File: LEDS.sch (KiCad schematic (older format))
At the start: 8 parts

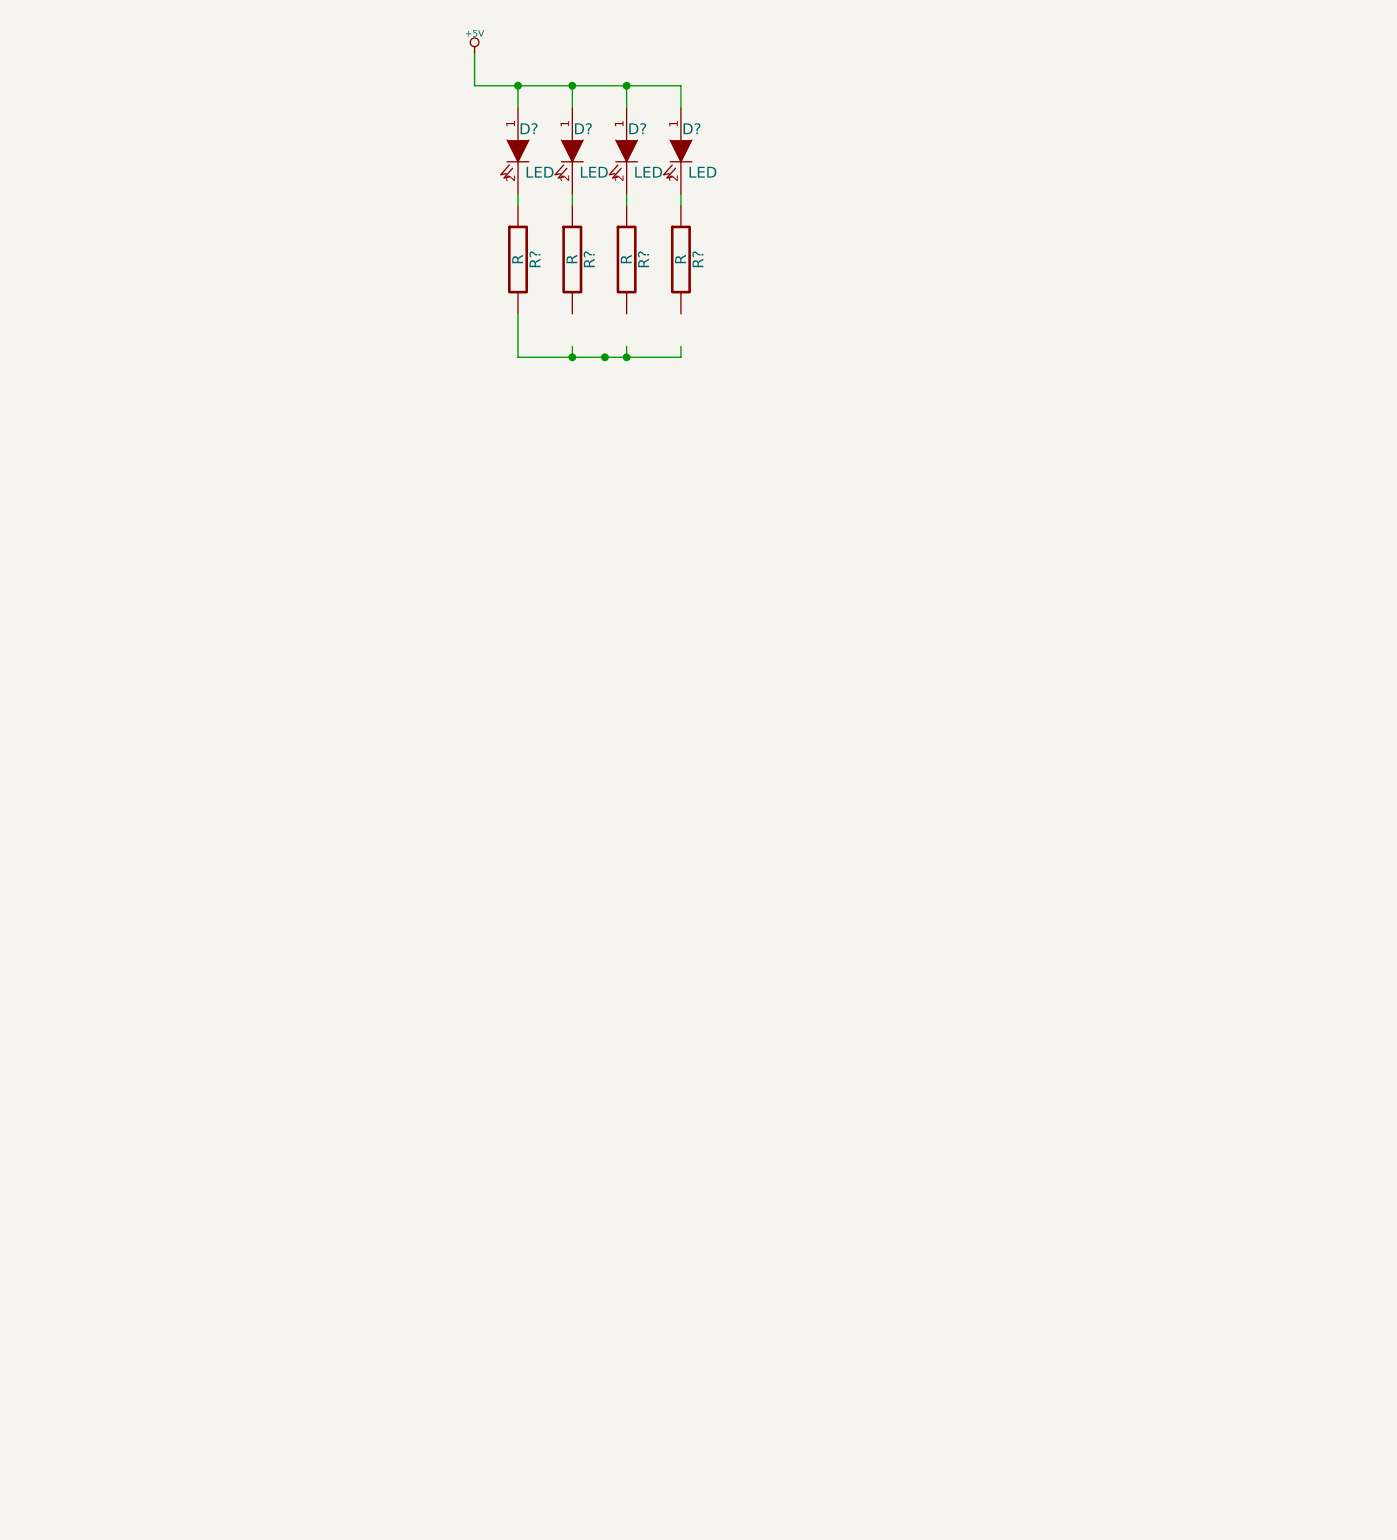
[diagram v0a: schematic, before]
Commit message: starting LED array, adjusting PCB
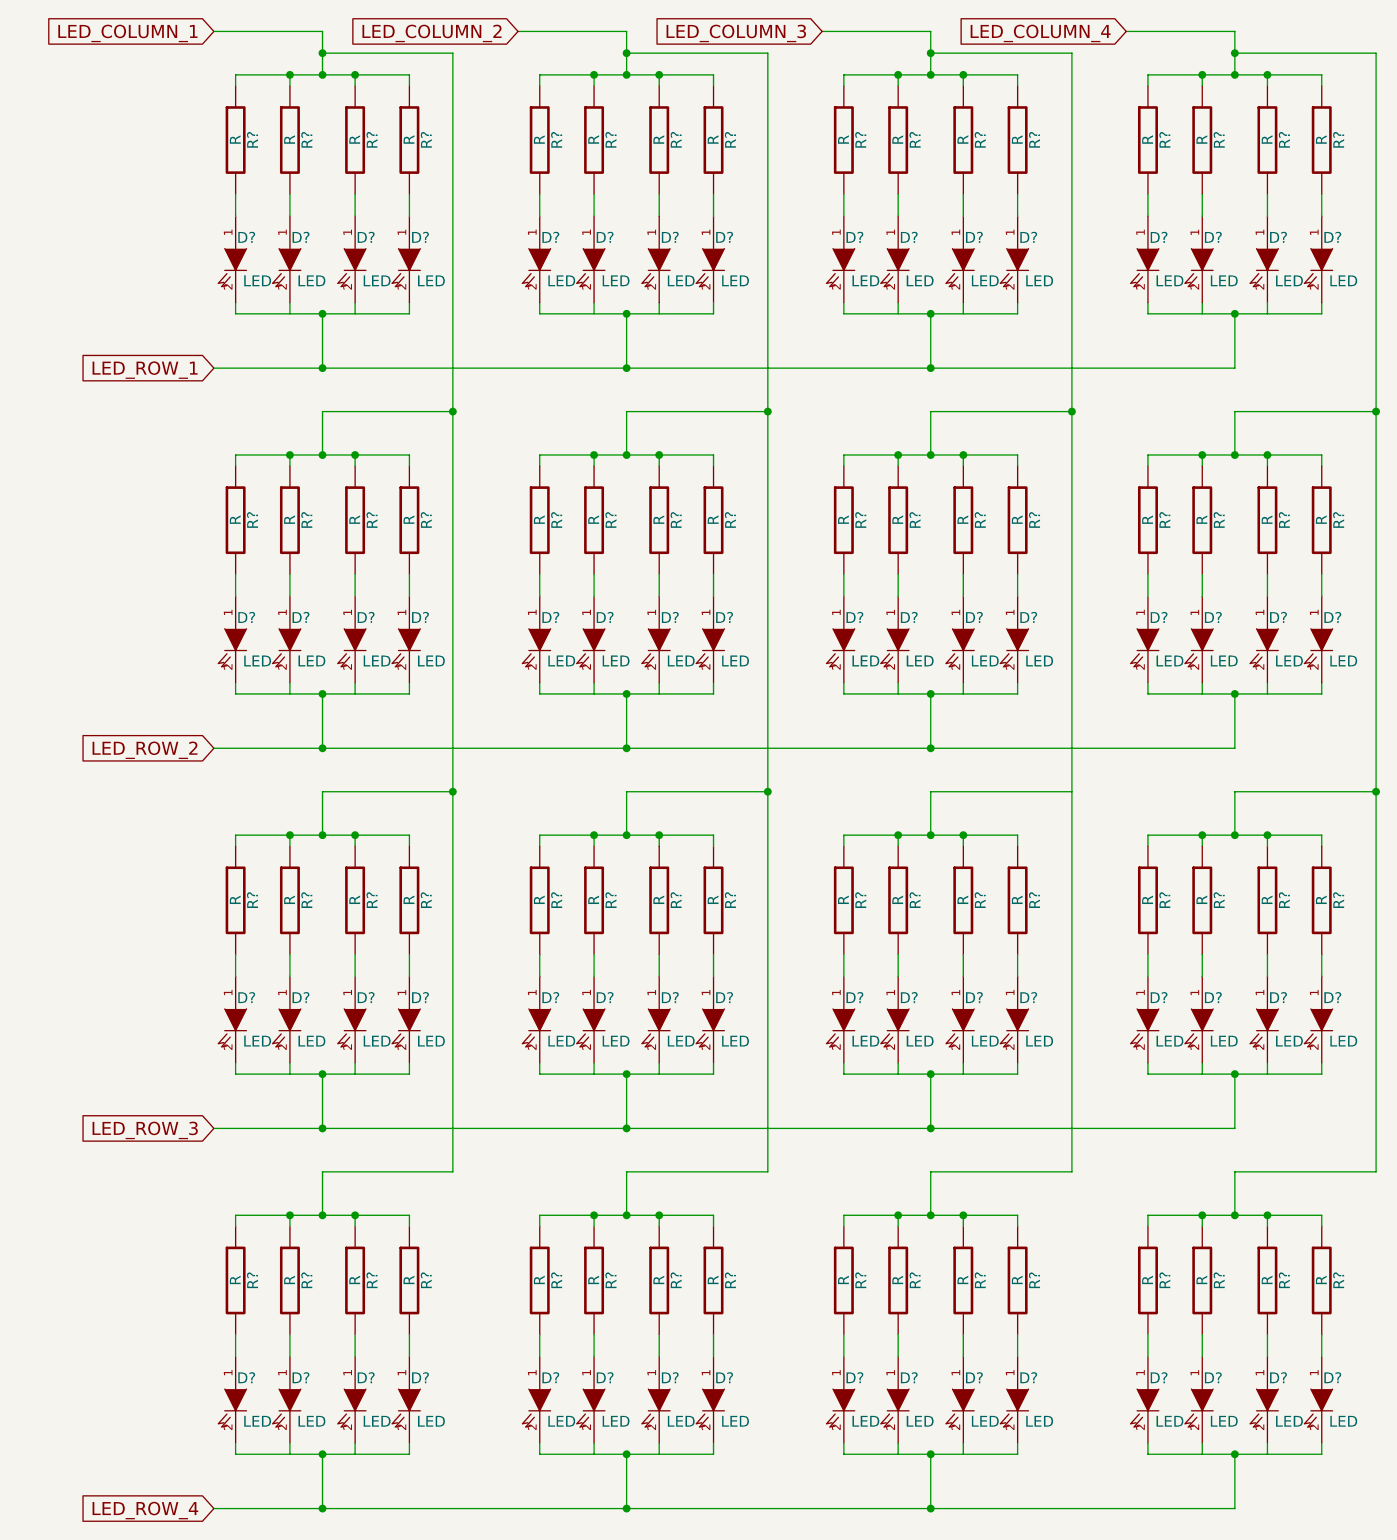
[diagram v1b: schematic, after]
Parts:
- added D? (x60): LED, symbol LED
- added R? (x60): R, symbol R
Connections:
- net labels added: LED_COLUMN_1, LED_COLUMN_2, LED_COLUMN_3, LED_COLUMN_4, LED_ROW_1, LED_ROW_2, LED_ROW_3, LED_ROW_4
- net labels removed: +5V
- wire segments 15 -> 284
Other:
- moved on the sheet: D?, R?

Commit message: working mainly on LEDs
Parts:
- R? (x64): value R -> 120R

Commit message: commiting before change to LED numbers
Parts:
- added JP?: JUMPER, symbol JUMPER
- added Q?: MOSFET_P, SOT323-MOS, symbol MOSFET_P
- added R?: 22R, symbol R
- added R?: 4k7, symbol R
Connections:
- net labels added: +5V, LED_COLUMN_1_SW, LED_COLUMN_2_SW, LED_COLUMN_3_SW, LED_COLUMN_4_SW, LED_ROW_1_SW, LED_ROW_2_SW, LED_ROW_3_SW, LED_ROW_4_SW
- net labels removed: LED_COLUMN_2, LED_COLUMN_3, LED_COLUMN_4, LED_ROW_1, LED_ROW_2, LED_ROW_3, LED_ROW_4
- wire segments 284 -> 416

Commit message: removing LEDs, adding switch
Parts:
- removed D? (x64): LED, symbol LED
- removed JP?: JUMPER, symbol JUMPER
- removed Q?: MOSFET_P, SOT323-MOS, symbol MOSFET_P
- removed R? (x64): 120R, symbol R
- removed R?: 22R, symbol R
- removed R?: 4k7, symbol R
- added D? (x16): LED, symbol LED
- added Q? (x4): MOSFET_N, symbol MOSFET_N
- added R? (x16): 120R, symbol R
- added R? (x4): 22R, symbol R
- added R? (x4): 4k7, symbol R
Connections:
- net labels added: GND, LED_COLUMN_2, LED_COLUMN_3, LED_COLUMN_4, LED_ROW_1, LED_ROW_2, LED_ROW_3, LED_ROW_4
- net labels removed: +5V, LED_COLUMN_1_SW, LED_COLUMN_2_SW, LED_COLUMN_3_SW, LED_COLUMN_4_SW
- wire segments 416 -> 112

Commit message: starting layout
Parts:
- added D10, D11, D12, D13, D18, D19, D2, D20, D21, D26, D27, D28, D29, D3, D4, D5: LED, symbol LED
- added R25, R26, R27, R28, R33, R34, R35, R36, R41, R42, R43, R44, R49, R50, R51, R52: 120R, symbol R
- gave numbers to parts that had none: 44
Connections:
- net LED_COLUMN_1: now also R25.1, R26.1, R27.1, R28.1
- net LED_COLUMN_2: now also R33.1, R34.1, R35.1, R36.1
- net LED_COLUMN_3: now also R41.1, R42.1, R43.1, R44.1
- net LED_COLUMN_4: now also R49.1, R50.1, R51.1, R52.1
- net LED_ROW_1_SW: now also D10.2 (K), D18.2 (K), D2.2 (K), D26.2 (K)
- net LED_ROW_2_SW: now also D11.2 (K), D19.2 (K), D27.2 (K), D3.2 (K)
- net LED_ROW_3_SW: now also D12.2 (K), D20.2 (K), D28.2 (K), D4.2 (K)
- net LED_ROW_4_SW: now also D13.2 (K), D21.2 (K), D29.2 (K), D5.2 (K)
- new net: D2.1 (A), R25.2
- new net: D10.1 (A), R33.2
- new net: D18.1 (A), R41.2
- new net: D26.1 (A), R49.2
- new net: D3.1 (A), R26.2
- new net: D11.1 (A), R34.2
- new net: D19.1 (A), R42.2
- new net: D27.1 (A), R50.2
- new net: D4.1 (A), R27.2
- new net: D12.1 (A), R35.2
- new net: D20.1 (A), R43.2
- new net: D28.1 (A), R51.2
- new net: D5.1 (A), R28.2
- new net: D13.1 (A), R36.2
- new net: D21.1 (A), R44.2
- new net: D29.1 (A), R52.2

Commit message: placing LEDS, working out laser cutting
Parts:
- D1: renamed from D2; footprint (none) -> KPJA-2107SURCK
- D10: renamed from D7; footprint (none) -> KPJA-2107SURCK
- D11: footprint (none) -> KPJA-2107SURCK
- D12: renamed from D15; footprint (none) -> KPJA-2107SURCK
- D13: renamed from D19; footprint (none) -> KPJA-2107SURCK
- D14: renamed from D23; footprint (none) -> KPJA-2107SURCK
- D15: renamed from D27; footprint (none) -> KPJA-2107SURCK
- D16: renamed from D31; footprint (none) -> KPJA-2107SURCK
- D17: renamed from D4; footprint (none) -> KPJA-2107SURCK
- D18: renamed from D8; footprint (none) -> KPJA-2107SURCK
- D19: renamed from D12; footprint (none) -> KPJA-2107SURCK
- D2: renamed from D6; footprint (none) -> KPJA-2107SURCK
- D20: renamed from D16; footprint (none) -> KPJA-2107SURCK
- D21: renamed from D20; footprint (none) -> KPJA-2107SURCK
- D22: renamed from D24; footprint (none) -> KPJA-2107SURCK
- D23: renamed from D28; footprint (none) -> KPJA-2107SURCK
- D24: renamed from D32; footprint (none) -> KPJA-2107SURCK
- D25: renamed from D5; footprint (none) -> KPJA-2107SURCK
- D26: renamed from D9; footprint (none) -> KPJA-2107SURCK
- D27: renamed from D13; footprint (none) -> KPJA-2107SURCK
- D28: renamed from D17; footprint (none) -> KPJA-2107SURCK
- D29: renamed from D21; footprint (none) -> KPJA-2107SURCK
- D3: renamed from D10; footprint (none) -> KPJA-2107SURCK
- D30: renamed from D25; footprint (none) -> KPJA-2107SURCK
- D31: renamed from D29; footprint (none) -> KPJA-2107SURCK
- D32: renamed from D33; footprint (none) -> KPJA-2107SURCK
- D4: renamed from D14; footprint (none) -> KPJA-2107SURCK
- D5: renamed from D18; footprint (none) -> KPJA-2107SURCK
- D6: renamed from D22; footprint (none) -> KPJA-2107SURCK
- D7: renamed from D26; footprint (none) -> KPJA-2107SURCK
- D8: renamed from D30; footprint (none) -> KPJA-2107SURCK
- D9: renamed from D3; footprint (none) -> KPJA-2107SURCK
- Q1, Q2, Q3, Q4: footprint (none) -> SOT23-NX7002AK
- R17, R18, R19, R20, R21, R22, R23, R24, R25, R56: footprint (none) -> SM0805
- R26: renamed from R29; footprint (none) -> SM0805
- R27: renamed from R33; footprint (none) -> SM0805
- R28: renamed from R37; footprint (none) -> SM0805
- R29: renamed from R41; footprint (none) -> SM0805
- R30: renamed from R45; footprint (none) -> SM0805
- R31: renamed from R49; footprint (none) -> SM0805
- R32: renamed from R53; footprint (none) -> SM0805
- R33: renamed from R26; footprint (none) -> SM0805
- R34: renamed from R30; footprint (none) -> SM0805
- R35: renamed from R34; footprint (none) -> SM0805
- R36: renamed from R38; footprint (none) -> SM0805
- R37: renamed from R42; footprint (none) -> SM0805
- R38: renamed from R46; footprint (none) -> SM0805
- R39: renamed from R50; footprint (none) -> SM0805
- R40: renamed from R54; footprint (none) -> SM0805
- R41: renamed from R27; footprint (none) -> SM0805
- R42: renamed from R31; footprint (none) -> SM0805
- R43: renamed from R35; footprint (none) -> SM0805
- R44: renamed from R39; footprint (none) -> SM0805
- R45: renamed from R43; footprint (none) -> SM0805
- R46: renamed from R47; footprint (none) -> SM0805
- R47: renamed from R51; footprint (none) -> SM0805
- R48: renamed from R55; footprint (none) -> SM0805
- R49: renamed from R28; footprint (none) -> SM0805
- R50: renamed from R32; footprint (none) -> SM0805
- R51: renamed from R36; footprint (none) -> SM0805
- R52: renamed from R40; footprint (none) -> SM0805
- R53: renamed from R44; footprint (none) -> SM0805
- R54: renamed from R48; footprint (none) -> SM0805
- R55: renamed from R52; footprint (none) -> SM0805
